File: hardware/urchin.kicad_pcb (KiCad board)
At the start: 2 copper layers, 19 parts, among them IC1 ATMEGA328PB-A, IC2 ATTINY85-S, P1 CONN_02X03, P2 USB_OTG, U1 CH340G, Y1 12M

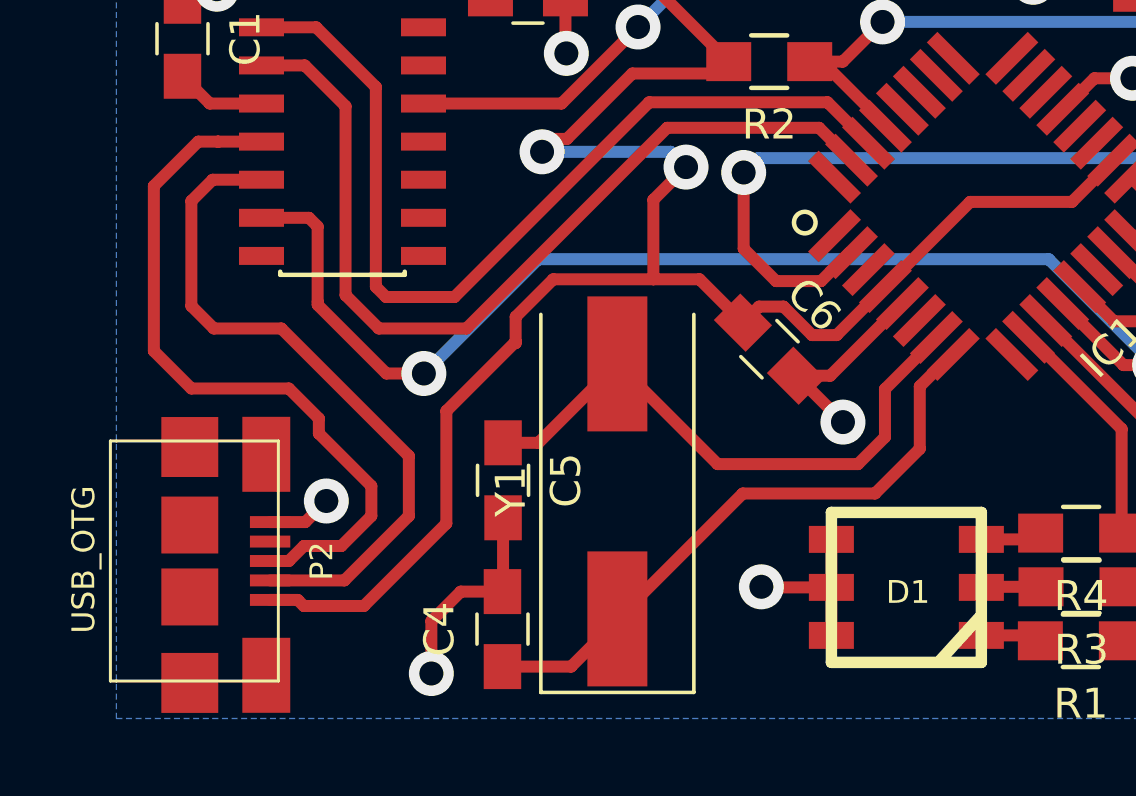
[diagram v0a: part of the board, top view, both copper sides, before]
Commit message: Adding keepout area below crystal.
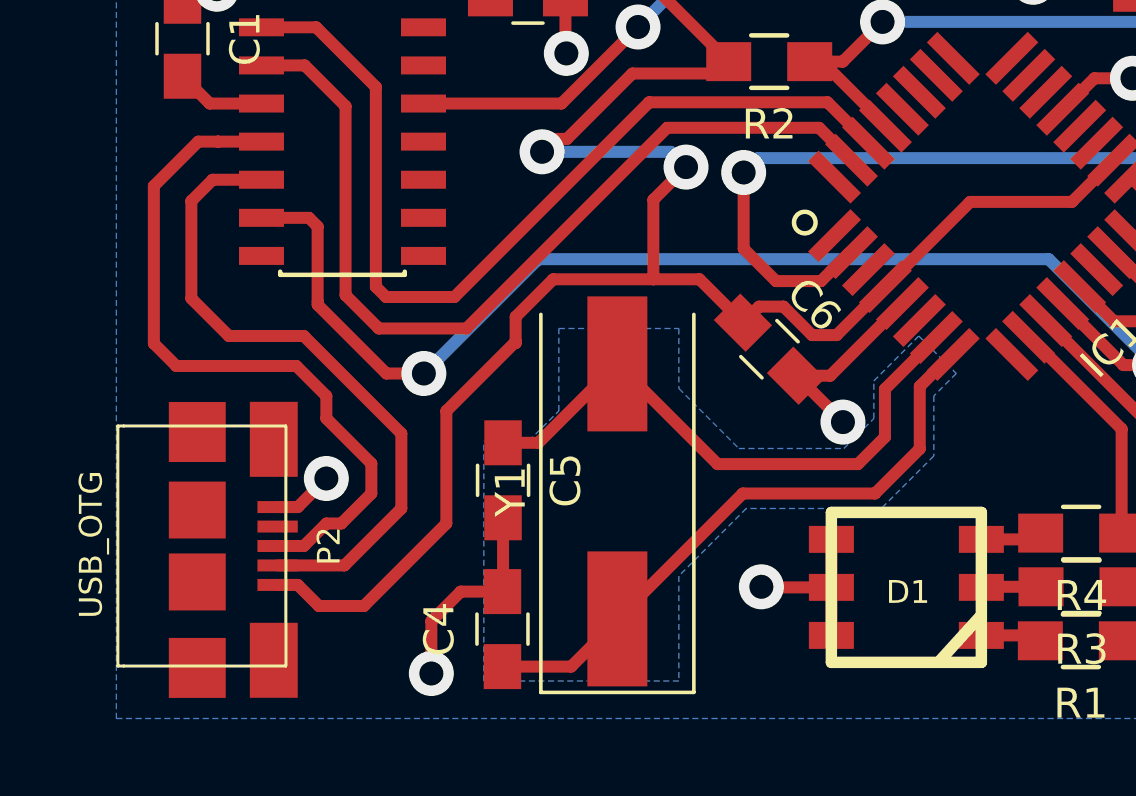
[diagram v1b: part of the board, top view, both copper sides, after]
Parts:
- moved P2 0.56 mm to (139.0, 86.2)
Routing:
- net Net-(P2-Pad2): track 23.0 -> 22.2 mm
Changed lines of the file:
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@@
   )
   (module urchin:MICRO-B_USB-INVERTED (layer F.Cu)
-    (at 138.75 86.75 270)
+    (at 139 86.25 270)
     (fp_text reference P2 (at 0 -5.842 270) (layer F.SilkS)
       (effects (font (size 0.762 0.762) (thickness 0.127)))
@@
     (pad "" smd rect (at -1.19888 -1.4478 270) (size 1.89738 1.89738) (layers F.Cu F.Paste F.Mask))
   )
-  (segment (start 142.87496 88.04794) (end 143.79794 88.04794) (width 0.4) (layer F.Cu) (net 1) (status 400000))
+  (segment (start 143.12496 87.54794) (end 143.79794 87.54794) (width 0.4) (layer F.Cu) (net 1) (status C00000))
+  (segment (start 143.79794 87.54794) (end 144.5 88.25) (width 0.4) (layer F.Cu) (net 1) (status 400000))
+  (segment (start 144.5 88.25) (end 146 88.25) (width 0.4) (layer F.Cu) (net 1))
   (segment (start 151.06 79.49) (end 151.06 78.61) (width 0.4) (layer F.Cu) (net 1))
   (segment (start 151.06 78.61) (end 152.31 77.36) (width 0.4) (layer F.Cu) (net 1))
@@
   (segment (start 148.75 85.5) (end 148.75 81.75) (width 0.4) (layer F.Cu) (net 1))
   (segment (start 146 88.25) (end 148.75 85.5) (width 0.4) (layer F.Cu) (net 1))
-  (segment (start 144 88.25) (end 146 88.25) (width 0.4) (layer F.Cu) (net 1))
-  (segment (start 143.79794 88.04794) (end 144 88.25) (width 0.4) (layer F.Cu) (net 1))
   (segment (start 179.578 76.62) (end 178.12 76.62) (width 0.4) (layer F.Cu) (net 1))
   (segment (start 187.192 82.562) (end 187.198 82.562) (width 0.4) (layer F.Cu) (net 1))
@@
   (segment (start 159.99 78.27) (end 159.172234 78.27) (width 0.4) (layer F.Cu) (net 1))
   (segment (start 159.172234 78.27) (end 158.636117 78.806117) (width 0.4) (layer F.Cu) (net 1))
-  (segment (start 142.87496 85.45206) (end 144.04794 85.45206) (width 0.4) (layer F.Cu) (net 2) (status 400000))
-  (via (at 144.75 84.75) (size 1.5) (drill 0.8) (layers F.Cu B.Cu) (net 2))
-  (segment (start 144.04794 85.45206) (end 144.75 84.75) (width 0.4) (layer F.Cu) (net 2))
-  (segment (start 150.62 87.77) (end 149.23 87.77) (width 0.4) (layer F.Cu) (net 2) (status 400000))
+  (segment (start 143.12496 84.95206) (end 143.79794 84.95206) (width 0.4) (layer F.Cu) (net 2) (status C00000))
+  (segment (start 143.79794 84.95206) (end 144.75 84) (width 0.4) (layer F.Cu) (net 2) (status 400000))
+  (via (at 144.75 84) (size 1.5) (drill 0.8) (layers F.Cu B.Cu) (net 2))
+  (segment (start 150.62 87.77) (end 149.23 87.77) (width 0.4) (layer F.Cu) (net 2))
   (via (at 148.25 90.5) (size 1.5) (drill 0.8) (layers F.Cu B.Cu) (net 2))
   (segment (start 148.25 88.75) (end 148.25 90.5) (width 0.4) (layer F.Cu) (net 2))
@@
   (segment (start 177.57 83.73) (end 176.04 83.73) (width 0.4) (layer F.Cu) (net 19))
   (segment (start 178.7 84.86) (end 177.57 83.73) (width 0.4) (layer F.Cu) (net 19))
-  (segment (start 142.87496 87.3977) (end 145.3523 87.3977) (width 0.4) (layer F.Cu) (net 20) (status 400000))
-  (segment (start 140.959 74.041) (end 142.588 74.041) (width 0.4) (layer F.Cu) (net 20) (status 800000))
+  (segment (start 143.12496 86.8977) (end 145.3523 86.8977) (width 0.4) (layer F.Cu) (net 20) (status 400000))
+  (segment (start 141.5 79.25) (end 140.25 78) (width 0.4) (layer F.Cu) (net 20))
+  (segment (start 144 79.25) (end 141.5 79.25) (width 0.4) (layer F.Cu) (net 20))
+  (segment (start 147.25 82.5) (end 144 79.25) (width 0.4) (layer F.Cu) (net 20))
+  (segment (start 147.25 85) (end 147.25 82.5) (width 0.4) (layer F.Cu) (net 20))
+  (segment (start 145.3523 86.8977) (end 147.25 85) (width 0.4) (layer F.Cu) (net 20))
+  (segment (start 140.959 74.041) (end 142.588 74.041) (width 0.4) (layer F.Cu) (net 20))
   (segment (start 140.25 74.75) (end 140.959 74.041) (width 0.4) (layer F.Cu) (net 20))
-  (segment (start 140.25 78.25) (end 140.25 74.75) (width 0.4) (layer F.Cu) (net 20))
-  (segment (start 141 79) (end 140.25 78.25) (width 0.4) (layer F.Cu) (net 20))
-  (segment (start 143.25 79) (end 141 79) (width 0.4) (layer F.Cu) (net 20))
-  (segment (start 147.5 83.25) (end 143.25 79) (width 0.4) (layer F.Cu) (net 20))
-  (segment (start 147.5 85.25) (end 147.5 83.25) (width 0.4) (layer F.Cu) (net 20))
-  (segment (start 145.3523 87.3977) (end 147.5 85.25) (width 0.4) (layer F.Cu) (net 20))
-  (segment (start 142.87496 86.75) (end 143.5 86.75) (width 0.4) (layer F.Cu) (net 21) (status C00000))
-  (segment (start 143.5 86.75) (end 144 86.25) (width 0.4) (layer F.Cu) (net 21) (status 400000))
-  (segment (start 144 86.25) (end 145.25 86.25) (width 0.4) (layer F.Cu) (net 21))
-  (segment (start 145.25 86.25) (end 146.25 85.25) (width 0.4) (layer F.Cu) (net 21))
-  (segment (start 146.25 85.25) (end 146.25 84.25) (width 0.4) (layer F.Cu) (net 21))
-  (segment (start 146.25 84.25) (end 144.5 82.5) (width 0.4) (layer F.Cu) (net 21))
-  (segment (start 144.5 82.5) (end 144.5 82) (width 0.4) (layer F.Cu) (net 21))
-  (segment (start 144.5 82) (end 143.5 81) (width 0.4) (layer F.Cu) (net 21))
-  (segment (start 143.5 81) (end 140.25 81) (width 0.4) (layer F.Cu) (net 21))
-  (segment (start 140.25 81) (end 139 79.75) (width 0.4) (layer F.Cu) (net 21))
-  (segment (start 139 79.75) (end 139 74.25) (width 0.4) (layer F.Cu) (net 21))
+  (segment (start 140.25 78) (end 140.25 74.75) (width 0.4) (layer F.Cu) (net 20))
+  (segment (start 143.12496 86.25) (end 144 86.25) (width 0.4) (layer F.Cu) (net 21) (status 400000))
+  (segment (start 139.75 80.25) (end 139 79.5) (width 0.4) (layer F.Cu) (net 21))
+  (segment (start 143.75 80.25) (end 139.75 80.25) (width 0.4) (layer F.Cu) (net 21))
+  (segment (start 144.75 81.25) (end 143.75 80.25) (width 0.4) (layer F.Cu) (net 21))
+  (segment (start 144.75 82) (end 144.75 81.25) (width 0.4) (layer F.Cu) (net 21))
+  (segment (start 146.25 83.5) (end 144.75 82) (width 0.4) (layer F.Cu) (net 21))
+  (segment (start 146.25 84.5) (end 146.25 83.5) (width 0.4) (layer F.Cu) (net 21))
+  (segment (start 145.25 85.5) (end 146.25 84.5) (width 0.4) (layer F.Cu) (net 21))
+  (segment (start 144.75 85.5) (end 145.25 85.5) (width 0.4) (layer F.Cu) (net 21))
+  (segment (start 144 86.25) (end 144.75 85.5) (width 0.4) (layer F.Cu) (net 21))
+  (segment (start 139 79.5) (end 139 74.25) (width 0.4) (layer F.Cu) (net 21))
   (segment (start 139 74.25) (end 140.479 72.771) (width 0.4) (layer F.Cu) (net 21))
   (segment (start 140.479 72.771) (end 141.139 72.771) (width 0.4) (layer F.Cu) (net 21))
@@
       )
     )
+    (polygon
+      (pts        (xy 150 82.75) (xy 151.5 82.75) (xy 152.5 81.75) (xy 152.5 79) (xy 156.5 79)
+        (xy 156.5 81) (xy 158.5 83) (xy 162 83) (xy 163 82) (xy 163 80.75)
+        (xy 164.5 79.25) (xy 165.75 80.5) (xy 165 81.25) (xy 165 83.25) (xy 163.25 85)
+        (xy 158.75 85) (xy 156.5 87.25) (xy 156.5 90.75) (xy 150 90.75)
+      )
+    )

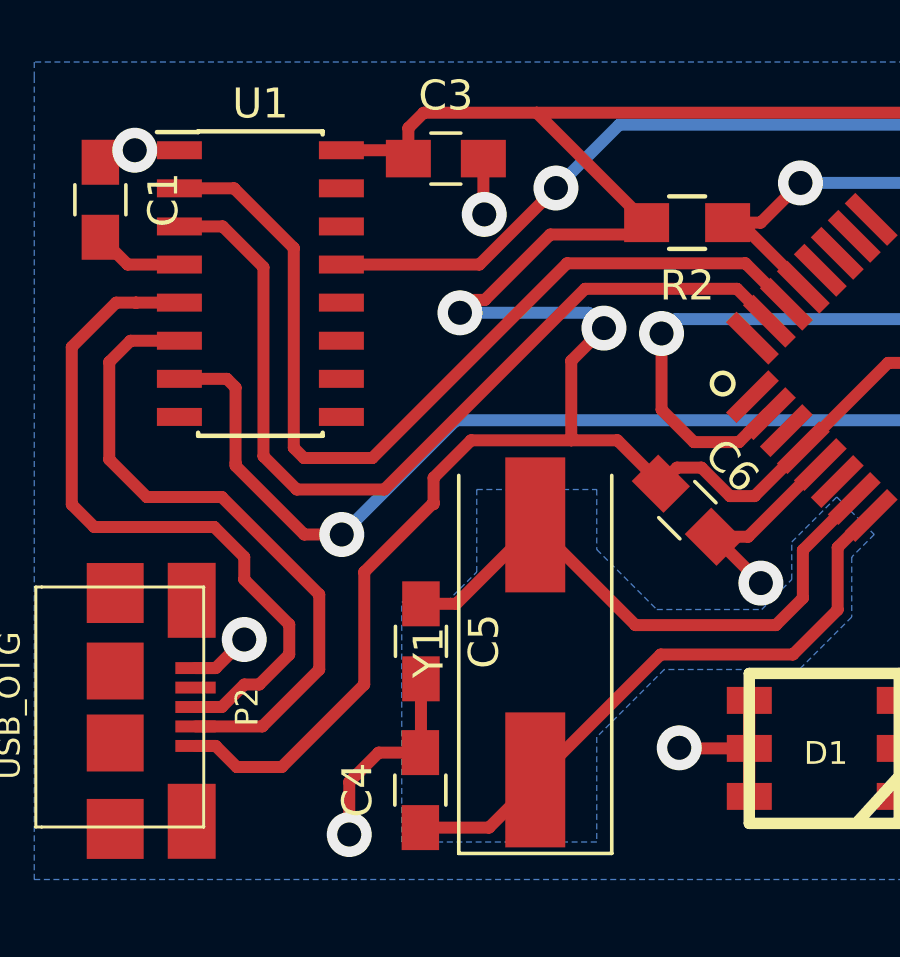
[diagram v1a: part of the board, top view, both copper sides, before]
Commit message: Adding alignment markers; plots.
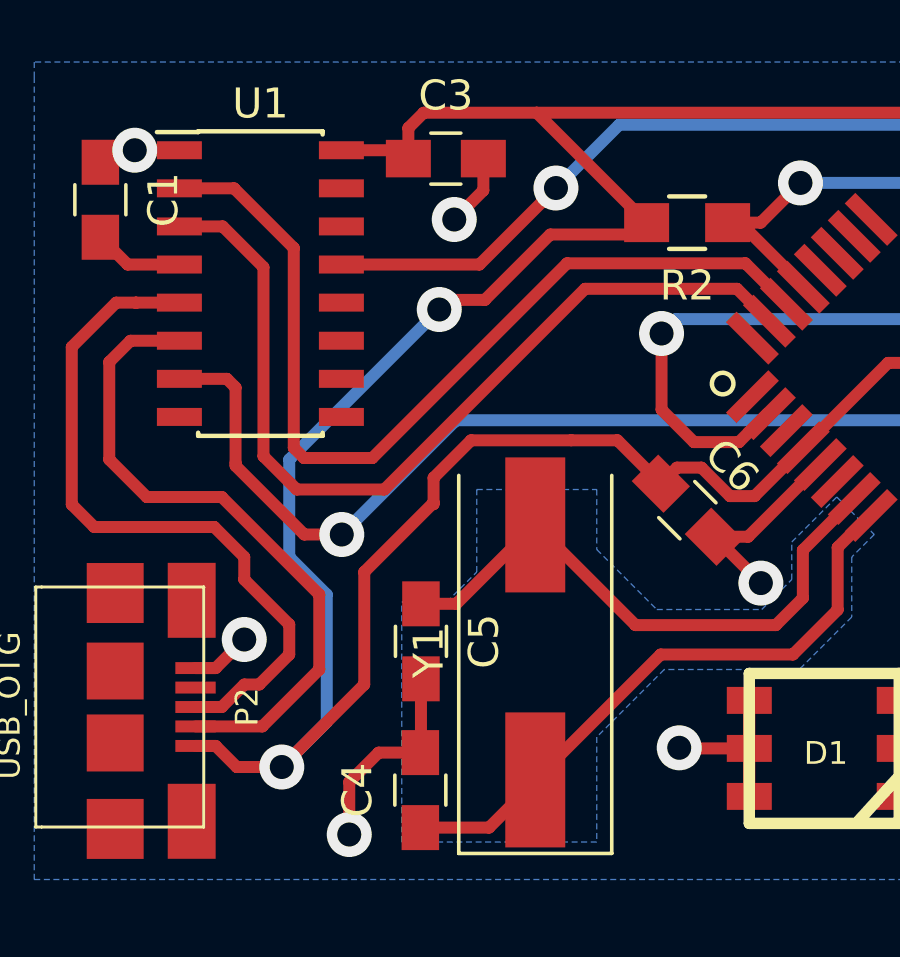
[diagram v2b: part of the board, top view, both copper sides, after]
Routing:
- net +5V: track 147.6 -> 157.5 mm
- net GND: track 36.8 -> 37.3 mm
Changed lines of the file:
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@@
     (area 0 0 0 0)
     (thickness 1.6)
-    (drawings 0)
-    (tracks 292)
+    (drawings 4)
+    (tracks 293)
     (zones 0)
     (modules 19)
@@
     (pad "" smd rect (at -1.19888 -1.4478 270) (size 1.89738 1.89738) (layers F.Cu F.Paste F.Mask))
   )
-  (segment (start 143.12496 87.54794) (end 143.79794 87.54794) (width 0.4) (layer F.Cu) (net 1) (status C00000))
-  (segment (start 143.79794 87.54794) (end 144.5 88.25) (width 0.4) (layer F.Cu) (net 1) (status 400000))
+  (target x (at 174.4 93.6) (size 3) (width 0.15) (layer Edge.Cuts))
+  (target plus (at 190.8 63.6) (size 5) (width 0.15) (layer Edge.Cuts))
+  (target plus (at 136.4 93.2) (size 5) (width 0.15) (layer Edge.Cuts))
+  (target plus (at 136.4 63.6) (size 5) (width 0.15) (layer Edge.Cuts))
+  (via (at 146 88.25) (size 1.5) (drill 0.8) (layers F.Cu B.Cu) (net 1))
+  (segment (start 157.766 70.5) (end 154.95 70.5) (width 0.4) (layer F.Cu) (net 1))
+  (segment (start 152.77 72.68) (end 154.95 70.5) (width 0.4) (layer F.Cu) (net 1))
+  (segment (start 151.57 72.68) (end 152.77 72.68) (width 0.4) (layer F.Cu) (net 1))
+  (segment (start 151.25 73) (end 151.57 72.68) (width 0.4) (layer F.Cu) (net 1))
+  (via (at 151.25 73) (size 1.5) (drill 0.8) (layers F.Cu B.Cu) (net 1))
+  (segment (start 146.25 78) (end 151.25 73) (width 0.4) (layer B.Cu) (net 1))
+  (segment (start 146.25 81.25) (end 146.25 78) (width 0.4) (layer B.Cu) (net 1))
+  (segment (start 147.5 82.5) (end 146.25 81.25) (width 0.4) (layer B.Cu) (net 1))
+  (segment (start 147.5 86.75) (end 147.5 82.5) (width 0.4) (layer B.Cu) (net 1))
+  (segment (start 147.5 86.75) (end 146 88.25) (width 0.4) (layer B.Cu) (net 1))
+  (segment (start 143.12496 87.54794) (end 143.79794 87.54794) (width 0.4) (layer F.Cu) (net 1))
+  (segment (start 143.79794 87.54794) (end 144.5 88.25) (width 0.4) (layer F.Cu) (net 1))
   (segment (start 144.5 88.25) (end 146 88.25) (width 0.4) (layer F.Cu) (net 1))
   (segment (start 151.06 79.49) (end 151.06 78.61) (width 0.4) (layer F.Cu) (net 1))
+  (segment (start 157.19 77.36) (end 158.636117 78.806117) (width 0.4) (layer F.Cu) (net 1))
+  (segment (start 155.65 77.36) (end 157.19 77.36) (width 0.4) (layer F.Cu) (net 1))
+  (segment (start 146 88.25) (end 148.75 85.5) (width 0.4) (layer F.Cu) (net 1))
+  (segment (start 148.75 85.5) (end 148.75 81.75) (width 0.4) (layer F.Cu) (net 1))
+  (segment (start 148.75 81.75) (end 151.06 79.44) (width 0.4) (layer F.Cu) (net 1))
+  (segment (start 151.06 79.44) (end 151.06 79.49) (width 0.4) (layer F.Cu) (net 1))
+  (segment (start 152.31 77.36) (end 155.65 77.36) (width 0.4) (layer F.Cu) (net 1))
   (segment (start 151.06 78.61) (end 152.31 77.36) (width 0.4) (layer F.Cu) (net 1))
-  (segment (start 152.31 77.36) (end 155.65 77.36) (width 0.4) (layer F.Cu) (net 1))
-  (segment (start 151.06 79.44) (end 151.06 79.49) (width 0.4) (layer F.Cu) (net 1))
-  (segment (start 148.75 81.75) (end 151.06 79.44) (width 0.4) (layer F.Cu) (net 1))
-  (segment (start 148.75 85.5) (end 148.75 81.75) (width 0.4) (layer F.Cu) (net 1))
-  (segment (start 146 88.25) (end 148.75 85.5) (width 0.4) (layer F.Cu) (net 1))
   (segment (start 179.578 76.62) (end 178.12 76.62) (width 0.4) (layer F.Cu) (net 1))
   (segment (start 187.192 82.562) (end 187.198 82.562) (width 0.4) (layer F.Cu) (net 1))
@@
   (segment (start 184.244 85.471) (end 187.091 85.471) (width 0.4) (layer F.Cu) (net 1))
   (segment (start 187.091 85.471) (end 187.198 85.364) (width 0.4) (layer F.Cu) (net 1))
-  (segment (start 155.65 77.36) (end 155.65 74.71) (width 0.4) (layer F.Cu) (net 1))
-  (segment (start 154.95 70.5) (end 157.766 70.5) (width 0.4) (layer F.Cu) (net 1))
-  (segment (start 152.77 72.68) (end 154.95 70.5) (width 0.4) (layer F.Cu) (net 1))
-  (segment (start 152.37 72.68) (end 152.77 72.68) (width 0.4) (layer F.Cu) (net 1))
-  (segment (start 151.94 73.11) (end 152.37 72.68) (width 0.4) (layer F.Cu) (net 1))
-  (via (at 151.94 73.11) (size 1.5) (drill 0.8) (layers F.Cu B.Cu) (net 1))
-  (segment (start 156.23 73.11) (end 151.94 73.11) (width 0.4) (layer B.Cu) (net 1))
-  (segment (start 156.74 73.62) (end 156.23 73.11) (width 0.4) (layer B.Cu) (net 1))
-  (via (at 156.74 73.62) (size 1.5) (drill 0.8) (layers F.Cu B.Cu) (net 1))
-  (segment (start 155.65 74.71) (end 156.74 73.62) (width 0.4) (layer F.Cu) (net 1))
   (segment (start 157.766 70.5) (end 158.162 70.104) (width 0.4) (layer F.Cu) (net 1))
-  (segment (start 155.65 77.36) (end 157.19 77.36) (width 0.4) (layer F.Cu) (net 1))
   (segment (start 150.22 67.97) (end 150.22 66.95) (width 0.4) (layer F.Cu) (net 1))
   (segment (start 154.498 66.44) (end 158.162 70.104) (width 0.4) (layer F.Cu) (net 1))
@@
   (segment (start 147.988 67.691) (end 149.941 67.691) (width 0.4) (layer F.Cu) (net 1))
   (segment (start 149.941 67.691) (end 150.22 67.97) (width 0.4) (layer F.Cu) (net 1))
-  (segment (start 157.19 77.36) (end 158.636117 78.806117) (width 0.4) (layer F.Cu) (net 1))
   (segment (start 163.385451 77.602864) (end 163.377136 77.602864) (width 0.4) (layer F.Cu) (net 1))
   (segment (start 163.377136 77.602864) (end 161.76 79.22) (width 0.4) (layer F.Cu) (net 1))
@@
   (segment (start 159.99 78.27) (end 159.172234 78.27) (width 0.4) (layer F.Cu) (net 1))
   (segment (start 159.172234 78.27) (end 158.636117 78.806117) (width 0.4) (layer F.Cu) (net 1))
-  (segment (start 143.12496 84.95206) (end 143.79794 84.95206) (width 0.4) (layer F.Cu) (net 2) (status C00000))
-  (segment (start 143.79794 84.95206) (end 144.75 84) (width 0.4) (layer F.Cu) (net 2) (status 400000))
+  (segment (start 152.72 67.97) (end 152.72 69.03) (width 0.4) (layer F.Cu) (net 2))
+  (via (at 151.75 70) (size 1.5) (drill 0.8) (layers F.Cu B.Cu) (net 2))
+  (segment (start 152.72 69.03) (end 151.75 70) (width 0.4) (layer F.Cu) (net 2))
+  (segment (start 143.12496 84.95206) (end 143.79794 84.95206) (width 0.4) (layer F.Cu) (net 2))
+  (segment (start 143.79794 84.95206) (end 144.75 84) (width 0.4) (layer F.Cu) (net 2))
   (via (at 144.75 84) (size 1.5) (drill 0.8) (layers F.Cu B.Cu) (net 2))
   (segment (start 150.62 87.77) (end 149.23 87.77) (width 0.4) (layer F.Cu) (net 2))
@@
   (via (at 141.1 67.691) (size 1.5) (drill 0.8) (layers F.Cu B.Cu) (net 2))
   (segment (start 141.1 67.691) (end 141.1 67.71) (width 0.4) (layer B.Cu) (net 2))
-  (segment (start 152.72 67.97) (end 152.72 69.8) (width 0.4) (layer F.Cu) (net 2))
-  (via (at 152.75 69.83) (size 1.5) (drill 0.8) (layers F.Cu B.Cu) (net 2))
-  (segment (start 152.72 69.8) (end 152.75 69.83) (width 0.4) (layer F.Cu) (net 2))
   (segment (start 142.588 67.691) (end 142.979 67.691) (width 0.4) (layer F.Cu) (net 2))
   (segment (start 139.954 68.092) (end 140.018 68.092) (width 0.4) (layer F.Cu) (net 2))
@@
   (segment (start 177.57 83.73) (end 176.04 83.73) (width 0.4) (layer F.Cu) (net 19))
   (segment (start 178.7 84.86) (end 177.57 83.73) (width 0.4) (layer F.Cu) (net 19))
-  (segment (start 143.12496 86.8977) (end 145.3523 86.8977) (width 0.4) (layer F.Cu) (net 20) (status 400000))
+  (segment (start 143.12496 86.8977) (end 145.3523 86.8977) (width 0.4) (layer F.Cu) (net 20))
   (segment (start 141.5 79.25) (end 140.25 78) (width 0.4) (layer F.Cu) (net 20))
   (segment (start 144 79.25) (end 141.5 79.25) (width 0.4) (layer F.Cu) (net 20))
@@
   (segment (start 140.25 74.75) (end 140.959 74.041) (width 0.4) (layer F.Cu) (net 20))
   (segment (start 140.25 78) (end 140.25 74.75) (width 0.4) (layer F.Cu) (net 20))
-  (segment (start 143.12496 86.25) (end 144 86.25) (width 0.4) (layer F.Cu) (net 21) (status 400000))
+  (segment (start 143.12496 86.25) (end 144 86.25) (width 0.4) (layer F.Cu) (net 21))
   (segment (start 139.75 80.25) (end 139 79.5) (width 0.4) (layer F.Cu) (net 21))
   (segment (start 143.75 80.25) (end 139.75 80.25) (width 0.4) (layer F.Cu) (net 21))

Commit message: Centering
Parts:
- moved U1 35.2 mm to (118.3, 94.7)
- moved C1 35.2 mm to (113.0, 91.9)
- moved C2 35.2 mm to (146.0, 90.4)
- moved C4 35.2 mm to (123.6, 111.6)
- moved C6 35.2 mm to (132.5, 102.3)
- moved D1 35.2 mm to (137.1, 110.2)
- moved R1 35.2 mm to (142.9, 112.0)
- moved R4 35.2 mm to (142.9, 108.4)
- moved C3 35.2 mm to (124.5, 90.6)
- moved C7 35.2 mm to (160.2, 109.2)
- moved IC1 35.2 mm to (139.6, 97.5)
- moved IC2 35.2 mm to (153.6, 110.0)
- moved JP1 35.2 mm to (152.6, 92.9)
- moved P1 35.2 mm to (155.1, 102.6)
- moved P2 35.2 mm to (112.0, 108.8)
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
